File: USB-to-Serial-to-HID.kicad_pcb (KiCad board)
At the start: 2 copper layers, 43.8 x 17.5 mm, 14 parts, among them J2 USB4520-03-1-A, J3 48037-2200, U1 CH340C, U2 CH9329

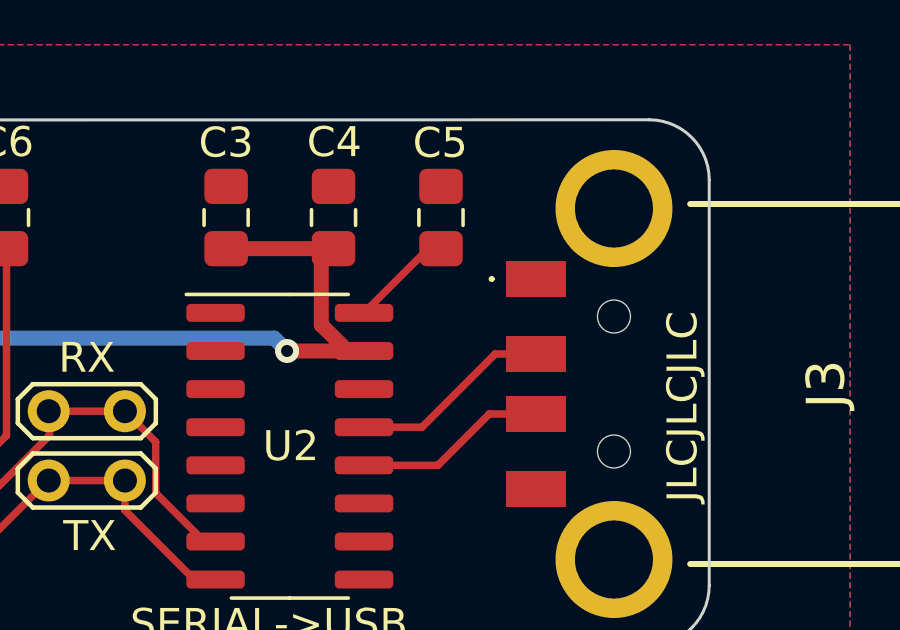
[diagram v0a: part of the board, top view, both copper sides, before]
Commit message: Update to use target 5V as well as host 5V
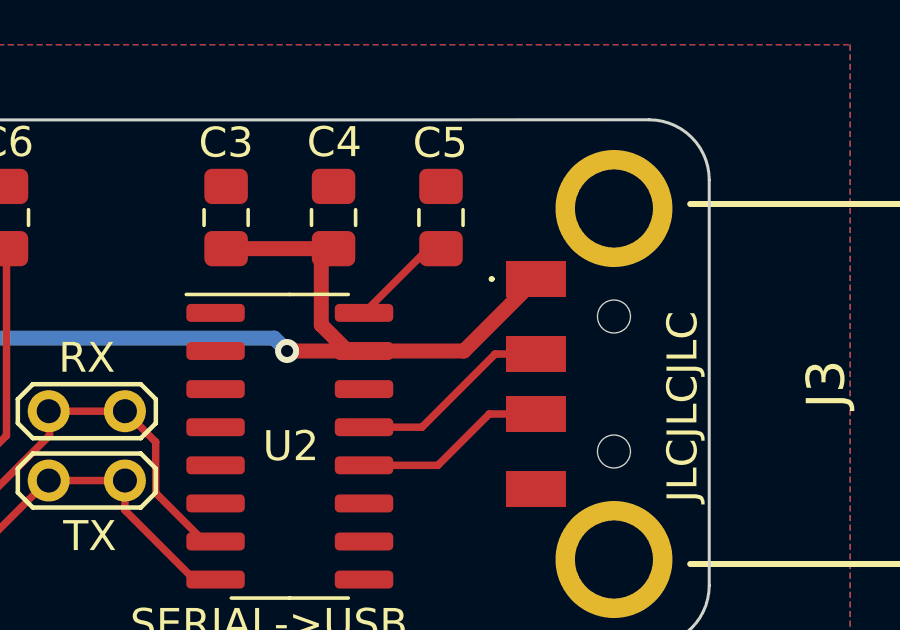
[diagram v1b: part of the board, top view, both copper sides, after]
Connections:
- J3 pad 1: unconnected-(J3-Pad1) -> USB_VIN
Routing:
- net USB_VIN: track 64.6 -> 71.4 mm
